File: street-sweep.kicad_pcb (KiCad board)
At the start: 2 copper layers, 110.6 x 91.3 mm, 61 parts, among them P1 GT-USB-7010ASV, P2 GT-USB-7010ASV, SW10 SW_Push, SW10_r1 SW_Push, SW11 SW_Push, SW11_r1 SW_Push, SW12 SW_Push, SW12_r1 SW_Push, SW13_r1 SW_Push, SW14 SW_Push, SW14_r1 SW_Push, SW15 SW_Push, SW15_r1 SW_Push, SW16 SW_Push, SW16_r1 SW_Push, SW17 SW_Push, SW17_r1 SW_Push, SW18 SW_Push, SW18_r1 SW_Push, SW2 SW_Push, SW20 SW_Push, SW21 SW_Push, SW2_r1 SW_Push, SW3 SW_Push, SW3_r1 SW_Push, SW4 SW_Push, SW4_r1 SW_Push, SW5 SW_Push, SW5_r1 SW_Push, SW6 SW_Push, SW6_r1 SW_Push, SW7_r1 SW_Push, SW8 SW_Push, SW8_r1 SW_Push, SW9 SW_Push, SW9_r1 SW_Push, U1 CH552G

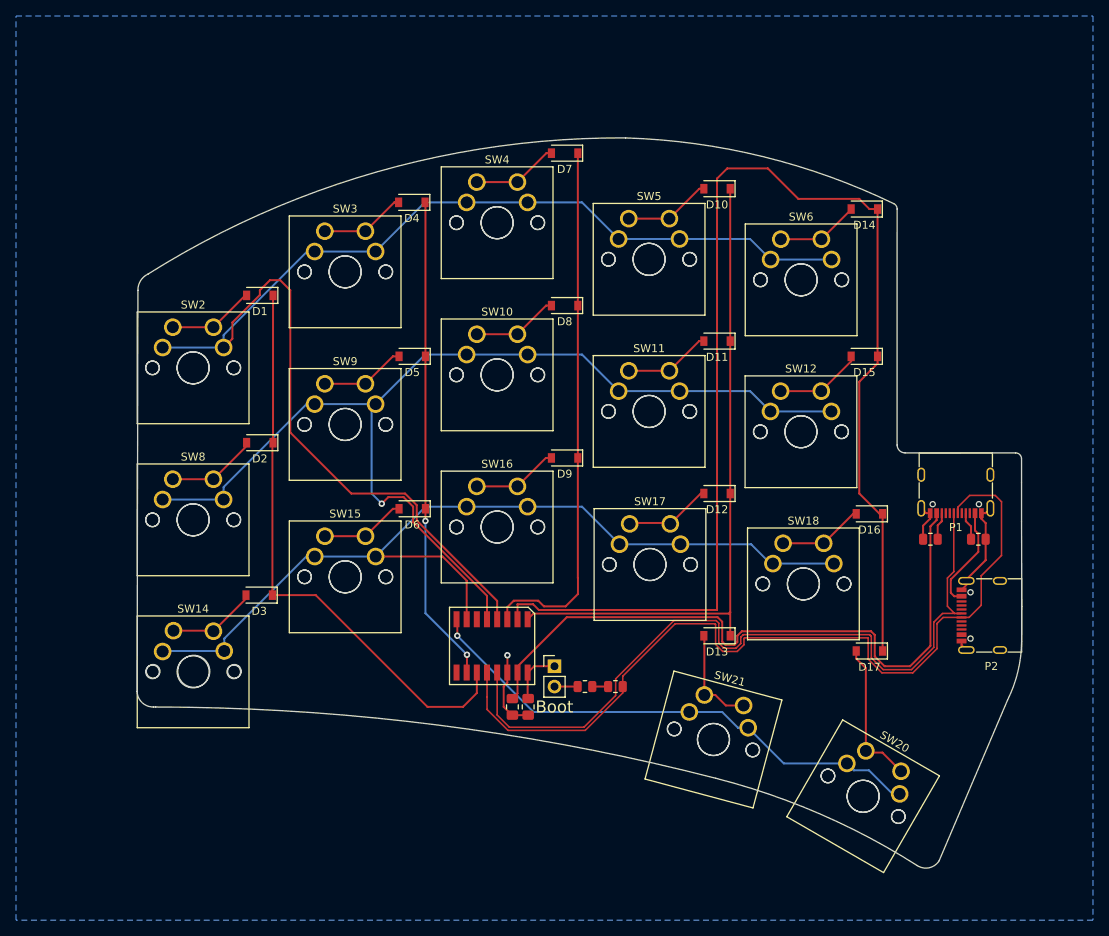
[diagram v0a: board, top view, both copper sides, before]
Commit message: Rotary Encoder added, still on CH552G
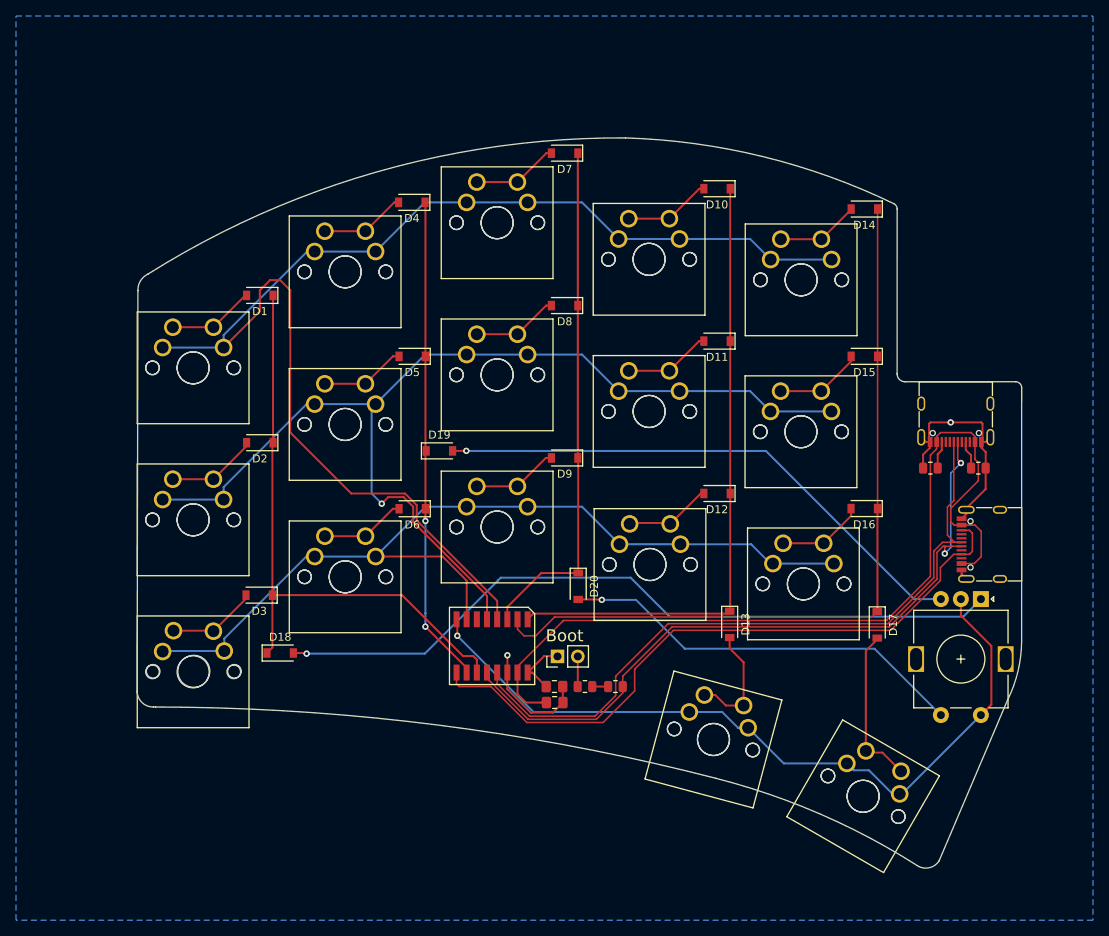
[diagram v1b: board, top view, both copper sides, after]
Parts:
- added D18: 1N4148, Diode_SMD:D_SOD-123, F.Cu at (53.3, 117.7)
- added D19: 1N4148, Diode_SMD:D_SOD-123, F.Cu at (73.2, 92.5)
- added D20: 1N4148, Diode_SMD:D_SOD-123, F.Cu at (90.6, 109.4)
- added SW1: RotaryEncoder_Switch, Rotary_Encoder:RotaryEncoder_Alps_EC11E-Switch_Vertical_H20mm, F.Cu at (140.9, 111.0)
- moved P1 8.89 mm to (137.8, 87.6)
- moved P2 8.89 mm to (142.2, 104.1)
- moved R1 8.89 mm to (134.6, 94.6)
- moved R2 8.89 mm to (140.6, 94.6)
- moved C1 5.31 mm to (87.7, 123.9), turned to 0 degrees
- moved C2 4.16 mm to (87.6, 121.9), turned to 0 degrees
- moved D17 3.41 mm to (128.0, 114.2), turned to -90 degrees
- moved D13 2.13 mm to (109.5, 114.1), turned to -90 degrees
- moved JP1 1.29 mm to (88.0, 118.2), turned to 90 degrees
- moved D16 0.92 mm to (126.4, 99.7)
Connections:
- P2 pad A5: unconnected-(P2-PadA5) -> serial
- P2 pad B5: unconnected-(P2-PadB5) -> serial
- U1 pad 9: unconnected-(U1-Pad9) -> serial
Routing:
- net Enc_A: track 0.00 -> 92.8 mm, vias 0 -> 1
- net serial: track 0.00 -> 83.1 mm
- net Enc_B: track 0.00 -> 68.7 mm, vias 0 -> 1
- net Column4: track 161.4 -> 98.0 mm
- net Switch18: track 0.00 -> 51.3 mm, vias 0 -> 1
- net Row3: track 65.6 -> 96.4 mm
- net D+: track 108.1 -> 90.2 mm, vias 0 -> 2
- net gnd: track 29.1 -> 45.3 mm, vias 1 -> 2
- net vcc: track 96.9 -> 109.4 mm
- net D-: track 96.2 -> 86.7 mm
- net Column0: track 72.1 -> 75.5 mm
- net Column3: track 81.6 -> 78.6 mm
- net Column2: track 66.7 -> 64.7 mm
- net Switch17: track 13.8 -> 15.6 mm
- net Switch16: track 18.4 -> 20.0 mm
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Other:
- outline, holes or cut-outs redrawn
